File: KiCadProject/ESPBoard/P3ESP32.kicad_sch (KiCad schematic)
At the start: 33 parts, among them SW301 SW_Push, SW302 SW_Push, U301 ESP32-S3-WROOM-1

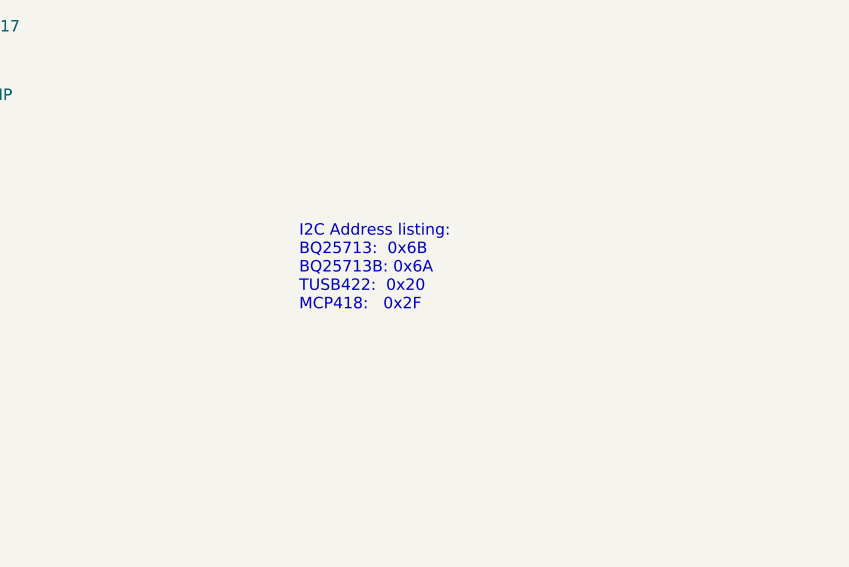
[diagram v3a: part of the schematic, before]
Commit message: Components selected, MfID added to schematics, and components ordered
Signed-off-by: Eldalote.Electronics <Eldalote.Electronics@gmail.com>
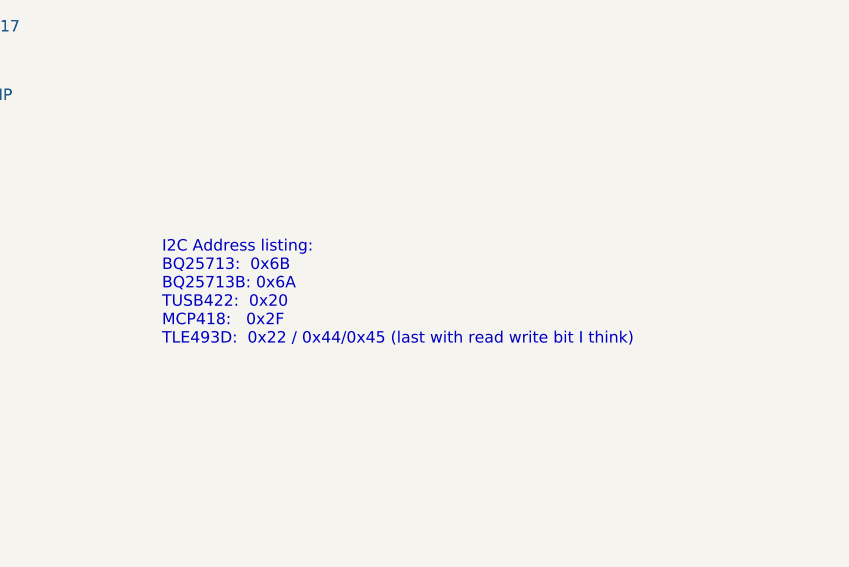
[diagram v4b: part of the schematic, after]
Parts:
- C301: MfID (none) -> CL21A106KAYNNNG
- C302, C304: MfID (none) -> CL05A104KA5NNNC
- C303: MfID (none) -> CL10A105KA8NNNC
- D301: footprint LED_SMD:LED_0603_1608Metric -> LED_SMD:LED_0805_2012Metric; MfID (none) -> APT2012SURCK
- D302: footprint LED_SMD:LED_0603_1608Metric -> LED_SMD:LED_0805_2012Metric; MfID (none) -> APT2012SYCK
- D303, D304, D305, D306, D307: footprint LED_SMD:LED_0603_1608Metric -> LED_SMD:LED_0805_2012Metric; MfID (none) -> APT2012CGCK
- R301: MfID (none) -> CR0402-FX-1002GLF
- R302, R305, R306, R307: MfID (none) -> CR0402-FX-1003GLF
- R303, R304: MfID (none) -> RMCF0402ZT0R00
- R308, R309, R310, R311, R312, R313, R314: MfID (none) -> CR0402-FX-2400GLF
- R318, R319: MfID (none) -> CR0402-FX-5101GLF
- SW301, SW302: MfID (none) -> PTS645SL43SMTR92 LFS
- U301: MfID (none) -> ESP32-S3-WROOM-1-N16
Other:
- note added: "I2C Address listing: BQ25713: 0x6B BQ25713B: 0x6A TUSB422: 0x20 MCP418: 0x2F TLE493D: 0x22 / 0x44/0x45 (last with read write bit I think)"
- note removed: "I2C Address listing: BQ25713: 0x6B BQ25713B: 0x6A TUSB422: 0x20 MCP418: 0x2F"
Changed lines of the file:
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@@
     (effects (font (size 1.27 1.27)) (justify left bottom))
   )
-  (text "I2C Address listing:\nBQ25713:  0x6B\nBQ25713B: 0x6A\nTUSB422:  0x20\nMCP418:   0x2F"
-    (at 227.33 140.97 0)
+  (text "I2C Address listing:\nBQ25713:  0x6B\nBQ25713B: 0x6A\nTUSB422:  0x20\nMCP418:   0x2F\nTLE493D:  0x22 / 0x44/0x45 (last with read write bit I think)"
+    (at 212.09 144.78 0)
     (effects (font (size 1.27 1.27)) (justify left bottom))
   )
@@
       (effects (font (size 1.27 1.27)) (justify right))
     )
-    (property "Footprint" "LED_SMD:LED_0603_1608Metric" (id 2) (at 245.11 48.26 0)
+    (property "Footprint" "LED_SMD:LED_0805_2012Metric" (id 2) (at 245.11 48.26 0)
       (effects (font (size 1.27 1.27)) hide)
     )
@@
       (effects (font (size 1.27 1.27)) hide)
     )
+    (property "MfID" "APT2012SYCK" (id 4) (at 245.11 48.26 0)
+      (effects (font (size 1.27 1.27)) hide)
+    )
     (pin "1")
     (pin "2")
@@
       (effects (font (size 1.27 1.27)) (justify right))
     )
-    (property "Footprint" "LED_SMD:LED_0603_1608Metric" (id 2) (at 245.11 38.1 0)
+    (property "Footprint" "LED_SMD:LED_0805_2012Metric" (id 2) (at 245.11 38.1 0)
       (effects (font (size 1.27 1.27)) hide)
     )
     (property "Datasheet" "~" (id 3) (at 245.11 38.1 0)
+      (effects (font (size 1.27 1.27)) hide)
+    )
+    (property "MfID" "APT2012SURCK" (id 4) (at 245.11 38.1 0)
       (effects (font (size 1.27 1.27)) hide)
     )
@@
       (effects (font (size 1.27 1.27)) (justify right))
     )
-    (property "Footprint" "LED_SMD:LED_0603_1608Metric" (id 2) (at 245.11 88.9 0)
+    (property "Footprint" "LED_SMD:LED_0805_2012Metric" (id 2) (at 245.11 88.9 0)
       (effects (font (size 1.27 1.27)) hide)
     )
@@
       (effects (font (size 1.27 1.27)) hide)
     )
+    (property "MfID" "APT2012CGCK" (id 4) (at 245.11 88.9 0)
+      (effects (font (size 1.27 1.27)) hide)
+    )
     (pin "1")
     (pin "2")
@@
       (effects (font (size 1.27 1.27)) (justify right))
     )
-    (property "Footprint" "LED_SMD:LED_0603_1608Metric" (id 2) (at 245.11 58.42 0)
+    (property "Footprint" "LED_SMD:LED_0805_2012Metric" (id 2) (at 245.11 58.42 0)
       (effects (font (size 1.27 1.27)) hide)
     )
     (property "Datasheet" "~" (id 3) (at 245.11 58.42 0)
+      (effects (font (size 1.27 1.27)) hide)
+    )
+    (property "MfID" "APT2012CGCK" (id 4) (at 245.11 58.42 0)
       (effects (font (size 1.27 1.27)) hide)
     )
@@
       (effects (font (size 1.27 1.27)) hide)
     )
+    (property "MfID" "CR0402-FX-2400GLF" (id 4) (at 254 58.42 0)
+      (effects (font (size 1.27 1.27)) hide)
+    )
     (pin "1")
     (pin "2")
@@
     )
     (property "Datasheet" "~" (id 3) (at 152.4 128.27 0)
+      (effects (font (size 1.27 1.27)) hide)
+    )
+    (property "MfID" "CR0402-FX-1003GLF" (id 4) (at 152.4 128.27 0)
       (effects (font (size 1.27 1.27)) hide)
     )
@@
     )
     (property "Datasheet" "~" (id 3) (at 157.48 74.93 0)
+      (effects (font (size 1.27 1.27)) hide)
+    )
+    (property "MfID" "RMCF0402ZT0R00" (id 4) (at 157.48 74.93 0)
       (effects (font (size 1.27 1.27)) hide)
     )
@@
       (effects (font (size 1.27 1.27)) hide)
     )
+    (property "MfID" "PTS645SL43SMTR92 LFS" (id 4) (at 54.61 48.26 0)
+      (effects (font (size 1.27 1.27)) hide)
+    )
     (pin "1")
     (pin "2")
@@
     )
     (property "Datasheet" "~" (id 3) (at 254 88.9 0)
+      (effects (font (size 1.27 1.27)) hide)
+    )
+    (property "MfID" "CR0402-FX-2400GLF" (id 4) (at 254 88.9 0)
       (effects (font (size 1.27 1.27)) hide)
     )
@@
     )
     (property "Datasheet" "~" (id 3) (at 160.02 128.27 0)
+      (effects (font (size 1.27 1.27)) hide)
+    )
+    (property "MfID" "CR0402-FX-1003GLF" (id 4) (at 160.02 128.27 0)
       (effects (font (size 1.27 1.27)) hide)
     )
@@
       (effects (font (size 1.27 1.27)) hide)
     )
+    (property "MfID" "PTS645SL43SMTR92 LFS" (id 4) (at 57.15 80.01 0)
+      (effects (font (size 1.27 1.27)) hide)
+    )
     (pin "1")
     (pin "2")
@@
       (effects (font (size 1.27 1.27)) hide)
     )
+    (property "MfID" "CR0402-FX-1003GLF" (id 4) (at 64.77 73.66 0)
+      (effects (font (size 1.27 1.27)) hide)
+    )
     (pin "1")
     (pin "2")
@@
     )
     (property "Datasheet" "~" (id 3) (at 63.5 53.34 0)
+      (effects (font (size 1.27 1.27)) hide)
+    )
+    (property "MfID" "CL10A105KA8NNNC" (id 4) (at 63.5 53.34 0)
       (effects (font (size 1.27 1.27)) hide)
     )
@@
   (symbol (lib_id "power:+3.3V") (at 209.55 66.04 0) (unit 1)
     (in_bom yes) (on_board yes) (fields_autoplaced)
-    (property "Reference" "#PWR?" (id 0) (at 209.55 69.85 0)
+    (property "Reference" "#PWR0111" (id 0) (at 209.55 69.85 0)
       (effects (font (size 1.27 1.27)) hide)
     )
@@
       (effects (font (size 1.27 1.27)) hide)
     )
+    (property "MfID" "CL05A104KA5NNNC" (id 4) (at 113.03 41.91 0)
+      (effects (font (size 1.27 1.27)) hide)
+    )
     (pin "1")
     (pin "2")
@@
       (effects (font (size 1.27 1.27)) hide)
     )
+    (property "MfID" "CR0402-FX-2400GLF" (id 4) (at 254 48.26 0)
+      (effects (font (size 1.27 1.27)) hide)
+    )
     (pin "1")
     (pin "2")
@@
       (effects (font (size 1.27 1.27)) (justify right))
     )
-    (property "Footprint" "LED_SMD:LED_0603_1608Metric" (id 2) (at 245.11 68.58 0)
+    (property "Footprint" "LED_SMD:LED_0805_2012Metric" (id 2) (at 245.11 68.58 0)
       (effects (font (size 1.27 1.27)) hide)
     )
@@
       (effects (font (size 1.27 1.27)) hide)
     )
+    (property "MfID" "APT2012CGCK" (id 4) (at 245.11 68.58 0)
+      (effects (font (size 1.27 1.27)) hide)
+    )
     (pin "1")
     (pin "2")
@@
       (effects (font (size 1.27 1.27)) hide)
     )
+    (property "MfID" "CR0402-FX-1003GLF" (id 4) (at 144.78 128.27 0)
+      (effects (font (size 1.27 1.27)) hide)
+    )
     (pin "1")
     (pin "2")
@@
       (effects (font (size 1.27 1.27)) hide)
     )
+    (property "MfID" "CR0402-FX-2400GLF" (id 4) (at 254 38.1 0)
+      (effects (font (size 1.27 1.27)) hide)
+    )
     (pin "1")
     (pin "2")
@@
     )
     (property "Datasheet" "~" (id 3) (at 102.87 41.91 0)
+      (effects (font (size 1.27 1.27)) hide)
+    )
+    (property "MfID" "CL21A106KAYNNNG" (id 4) (at 102.87 41.91 0)
       (effects (font (size 1.27 1.27)) hide)
     )
@@
     )
     (property "Datasheet" "" (id 3) (at 119.38 95.25 0)
+      (effects (font (size 1.27 1.27)) hide)
+    )
+    (property "MfID" "ESP32-S3-WROOM-1-N16" (id 4) (at 119.38 95.25 0)
       (effects (font (size 1.27 1.27)) hide)
     )
@@
       (effects (font (size 1.27 1.27)) hide)
     )
+    (property "MfID" "CR0402-FX-1002GLF" (id 4) (at 63.5 41.91 0)
+      (effects (font (size 1.27 1.27)) hide)
+    )
     (pin "1")
     (pin "2")
@@
     )
     (property "Datasheet" "~" (id 3) (at 254 78.74 0)
+      (effects (font (size 1.27 1.27)) hide)
+    )
+    (property "MfID" "CR0402-FX-2400GLF" (id 4) (at 254 78.74 0)
       (effects (font (size 1.27 1.27)) hide)
     )
@@
       (effects (font (size 1.27 1.27)) hide)
     )
+    (property "MfID" "RMCF0402ZT0R00" (id 4) (at 148.59 72.39 0)
+      (effects (font (size 1.27 1.27)) hide)
+    )
     (pin "1")
     (pin "2")
@@
       (effects (font (size 1.27 1.27)) hide)
     )
+    (property "MfID" "CL05A104KA5NNNC" (id 4) (at 57.15 85.09 0)
+      (effects (font (size 1.27 1.27)) hide)
+    )
     (pin "1")
     (pin "2")
@@
       (effects (font (size 1.27 1.27)) hide)
     )
+    (property "MfID" "CR0402-FX-2400GLF" (id 4) (at 254 68.58 0)
+      (effects (font (size 1.27 1.27)) hide)
+    )
     (pin "1")
     (pin "2")
@@
       (effects (font (size 1.27 1.27)) (justify right))
     )
-    (property "Footprint" "LED_SMD:LED_0603_1608Metric" (id 2) (at 245.11 99.06 0)
+    (property "Footprint" "LED_SMD:LED_0805_2012Metric" (id 2) (at 245.11 99.06 0)
       (effects (font (size 1.27 1.27)) hide)
     )
     (property "Datasheet" "~" (id 3) (at 245.11 99.06 0)
+      (effects (font (size 1.27 1.27)) hide)
+    )
+    (property "MfID" "APT2012CGCK" (id 4) (at 245.11 99.06 0)
       (effects (font (size 1.27 1.27)) hide)
     )
@@
       (effects (font (size 1.27 1.27)) hide)
     )
+    (property "MfID" "CR0402-FX-5101GLF" (id 4) (at 204.47 74.93 0)
+      (effects (font (size 1.27 1.27)) hide)
+    )
     (pin "1")
     (pin "2")
@@
       (effects (font (size 1.27 1.27)) hide)
     )
+    (property "MfID" "CR0402-FX-5101GLF" (id 4) (at 213.36 74.93 0)
+      (effects (font (size 1.27 1.27)) hide)
+    )
     (pin "1")
     (pin "2")
@@
       (effects (font (size 1.27 1.27)) hide)
     )
+    (property "MfID" "CR0402-FX-2400GLF" (id 4) (at 254 99.06 0)
+      (effects (font (size 1.27 1.27)) hide)
+    )
     (pin "1")
     (pin "2")
@@
       (effects (font (size 1.27 1.27)) (justify right))
     )
-    (property "Footprint" "LED_SMD:LED_0603_1608Metric" (id 2) (at 245.11 78.74 0)
+    (property "Footprint" "LED_SMD:LED_0805_2012Metric" (id 2) (at 245.11 78.74 0)
       (effects (font (size 1.27 1.27)) hide)
     )
@@
       (effects (font (size 1.27 1.27)) hide)
     )
+    (property "MfID" "APT2012CGCK" (id 4) (at 245.11 78.74 0)
+      (effects (font (size 1.27 1.27)) hide)
+    )

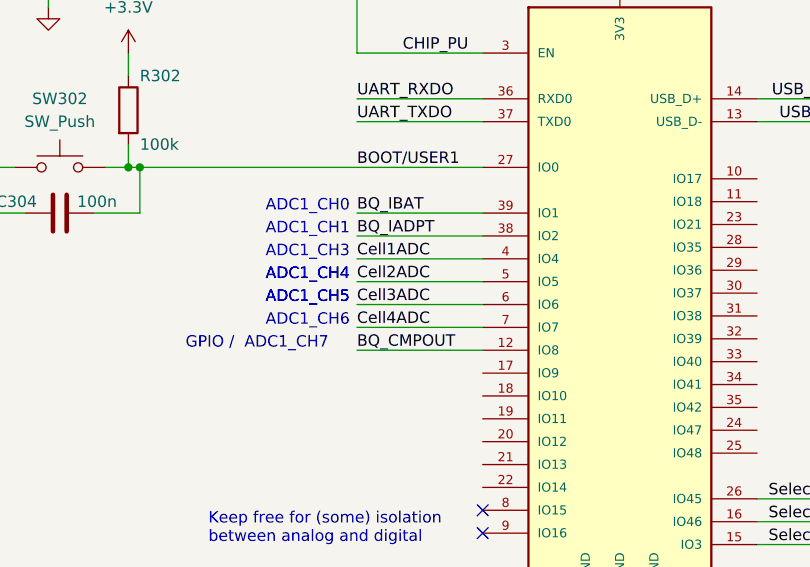
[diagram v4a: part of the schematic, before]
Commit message: Finished v0.1 of BatMan PCB, started layout of ESP PCB
Signed-off-by: Eldalote.Electronics <Eldalote.Electronics@gmail.com>
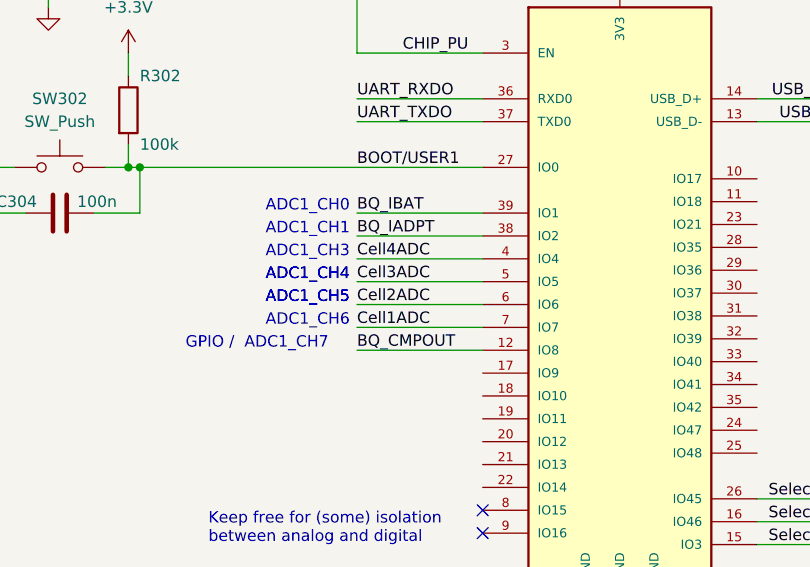
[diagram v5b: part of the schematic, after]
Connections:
- net Cell1ADC: now also U301.7 (IO7); no longer U301.4 (IO4)
- net Cell2ADC: now also U301.6 (IO6); no longer U301.5 (IO5)
- net Cell3ADC: now also U301.5 (IO5); no longer U301.6 (IO6)
- net Cell4ADC: now also U301.4 (IO4); no longer U301.7 (IO7)
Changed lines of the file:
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@@
+    (effects (font (size 1.27 1.27)) (justify left bottom))
+  )
+  (label "Cell2ADC" (at 90.17 95.25 0)
     (effects (font (size 1.27 1.27)) (justify left bottom))
   )
@@
   )
   (label "BQ_IBAT" (at 36.83 163.83 0)
-    (effects (font (size 1.27 1.27)) (justify left bottom))
-  )
-  (label "Cell4ADC" (at 90.17 97.79 0)
     (effects (font (size 1.27 1.27)) (justify left bottom))
   )
@@
   )
   (label "C_USB_D+" (at 36.83 172.72 0)
+    (effects (font (size 1.27 1.27)) (justify left bottom))
+  )
+  (label "Cell3ADC" (at 90.17 92.71 0)
     (effects (font (size 1.27 1.27)) (justify left bottom))
   )
@@
   )
   (label "Select 3" (at 135.89 121.92 0)
-    (effects (font (size 1.27 1.27)) (justify left bottom))
-  )
-  (label "Cell2ADC" (at 90.17 92.71 0)
     (effects (font (size 1.27 1.27)) (justify left bottom))
   )
@@
     (effects (font (size 1.27 1.27)) (justify left bottom))
   )
-  (label "Cell1ADC" (at 90.17 90.17 0)
-    (effects (font (size 1.27 1.27)) (justify left bottom))
-  )
   (label "BQ_CHRG_OK" (at 36.83 158.75 0)
     (effects (font (size 1.27 1.27)) (justify left bottom))
@@
     (effects (font (size 1.27 1.27)) (justify left bottom))
   )
+  (label "Cell1ADC" (at 90.17 97.79 0)
+    (effects (font (size 1.27 1.27)) (justify left bottom))
+  )
   (label "Cell3ADC" (at 77.47 176.53 0)
     (effects (font (size 1.27 1.27)) (justify left bottom))
   )
   (label "BQ_CMPOUT" (at 36.83 168.91 0)
+    (effects (font (size 1.27 1.27)) (justify left bottom))
+  )
+  (label "Cell4ADC" (at 90.17 90.17 0)
     (effects (font (size 1.27 1.27)) (justify left bottom))
   )
@@
     (effects (font (size 1.27 1.27)) (justify left bottom))
   )
-  (label "Cell3ADC" (at 90.17 95.25 0)
-    (effects (font (size 1.27 1.27)) (justify left bottom))
-  )

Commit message: Finished V0.1 of ESP PCB
Signed-off-by: Eldalote.Electronics <Eldalote.Electronics@gmail.com>
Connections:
- net BQ_CHRG_OK: now also U301.32 (IO39)
- net BQ_CMPOUT: now also U301.8 (IO15); no longer U301.12 (IO8)
- net BQ_EN_OTG: now also U301.17 (IO9)
- net BQ_IADPT: now also U301.9 (IO16); no longer U301.38 (IO2)
- net BQ_IBAT: now also U301.10 (IO17); no longer U301.39 (IO1)
- net Cell1Balance: now also U301.39 (IO1)
- net Cell2Balance: now also U301.38 (IO2)
- net Cell3Balance: now also U301.34 (IO41)
- net Cell4Balance: now also U301.35 (IO42)
- net GND: now also U301.41 (GND); no longer U301.41_1 (GND), U301.41_2 (GND), U301.41_3 (GND), U301.41_4 (GND), U301.41_5 (GND), U301.41_6 (GND), U301.41_7 (GND), U301.41_8 (GND), U301.41_9 (GND)
- net I2C_SCL: now also U301.30 (IO37)
- net I2C_SDA: now also U301.29 (IO36)
- net LED0: now also U301.20 (IO12)
- net LED1: now also U301.21 (IO13)
- net LED2: now also U301.22 (IO14)
- net LED3: now also U301.23 (IO21)
- net LED4: now also U301.24 (IO47)
- net LED5: now also U301.25 (IO48)
- net LED6: now also U301.28 (IO35)
- net MAINLED_PWM: now also U301.18 (IO10)
- net MAINLED_nFTL: now also U301.19 (IO11)
- net USBPD_INT_N: now also U301.31 (IO38)
- net USBPD_PTN_ID: now reaches U301.33 (IO40)
- net +3.3V renamed +3V3
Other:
- note added: "ADC2_CH4"
- note added: "ADC2_CH5"
- note added: "ADC2_CH6 / GPIO"
- note added: "Keep 11&12 free for (some) isolation between analog and digital"
- note removed: "ADC1_CH0"
- note removed: "ADC1_CH1"
- note removed: "GPIO / ADC1_CH7"
- note removed: "Keep free for (some) isolation between analog and digital"
- moved on the sheet: R318, R319

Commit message: Made ready to order PCBs. Some problems with ordering due to misunderstanding. Thinking about solutions
Signed-off-by: Eldalote.Electronics <Eldalote.Electronics@gmail.com>
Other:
- company: (none) -> Eldalote Electronics
- title: (none) -> ESP & Feedback Board
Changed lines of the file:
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@@
 (kicad_sch (version 20211123) (generator eeschema)
   (paper "A4")
+  (title_block
+    (title "ESP & Feedback Board")
+    (date "2023-02-02")
+    (rev "0.2")
+    (company "Eldalote Electronics")
+    (comment 2 "Part of the Dive Lamp Design")
+  )
   (junction (at 113.03 35.56) (diameter 0) (color 0 0 0 0)
   )
